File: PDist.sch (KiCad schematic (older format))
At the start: 27 parts

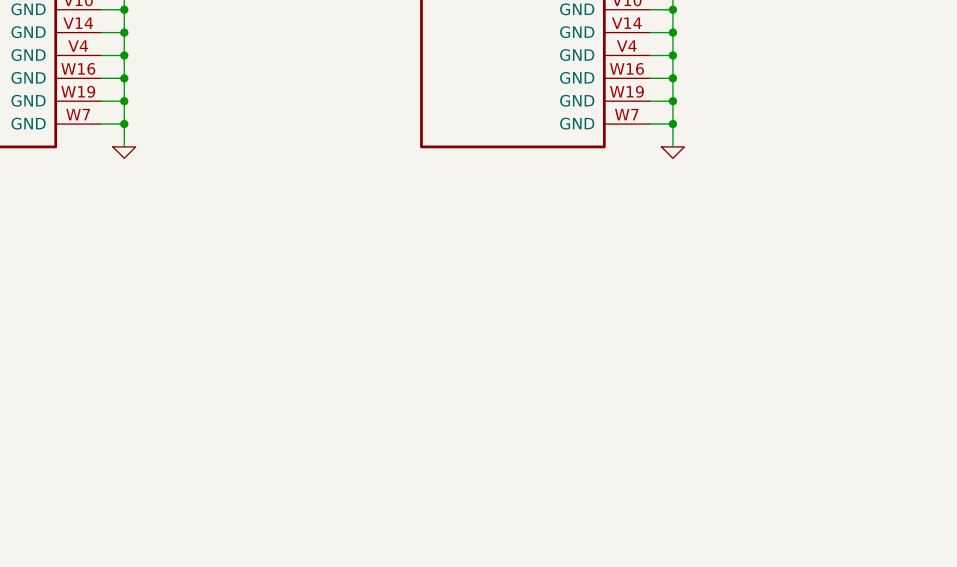
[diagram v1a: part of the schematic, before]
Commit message: Route CPU bus and cache
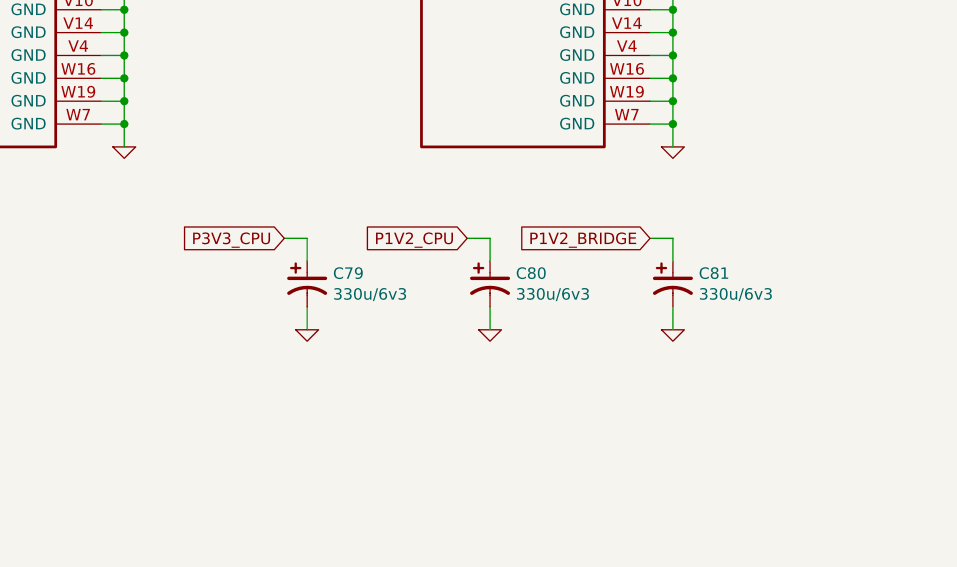
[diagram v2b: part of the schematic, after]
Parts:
- added C79, C80, C81: 330u/6v3, IPC7351-Nominal:CAPMP6032X280, symbol C-TANT-6032-28
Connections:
- net GND: now also C79.2, C80.2, C81.2
- net P1V2_BRIDGE: now also C81.1
- net P1V2_CPU: now also C80.1
- net P3V3_CPU: now also C79.1
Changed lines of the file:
@@
 $EndComp
 $Comp
-L GND #PWR7
+L GND #PWR10
 U 1 1 57647804
 P 1200 6200
-F 0 "#PWR7" H 1200 6200 30  0001 C CNN
+F 0 "#PWR10" H 1200 6200 30  0001 C CNN
 F 1 "GND" H 1200 6130 30  0001 C CNN
 F 2 "" H 1200 6200 60  0000 C CNN
@@
 	6000 6800 5900 6800
 $Comp
-L GND #PWR12
+L GND #PWR15
 U 1 1 57685CC5
 P 6000 6900
-F 0 "#PWR12" H 6000 6900 30  0001 C CNN
+F 0 "#PWR15" H 6000 6900 30  0001 C CNN
 F 1 "GND" H 6000 6830 30  0001 C CNN
 F 2 "" H 6000 6900 60  0000 C CNN
@@
 Connection ~ 2800 7200
 $Comp
-L GND #PWR8
+L GND #PWR11
 U 1 1 5781AB87
 P 1200 7300
-F 0 "#PWR8" H 1200 7300 30  0001 C CNN
+F 0 "#PWR11" H 1200 7300 30  0001 C CNN
 F 1 "GND" H 1200 7230 30  0001 C CNN
 F 2 "" H 1200 7300 60  0000 C CNN
@@
 Connection ~ 2800 7800
 $Comp
-L GND #PWR9
+L GND #PWR12
 U 1 1 5781BEBF
 P 1200 7900
-F 0 "#PWR9" H 1200 7900 30  0001 C CNN
+F 0 "#PWR12" H 1200 7900 30  0001 C CNN
 F 1 "GND" H 1200 7830 30  0001 C CNN
 F 2 "" H 1200 7900 60  0000 C CNN
@@
 Connection ~ 2800 8400
 $Comp
-L GND #PWR10
+L GND #PWR13
 U 1 1 5781BFF0
 P 1200 8500
-F 0 "#PWR10" H 1200 8500 30  0001 C CNN
+F 0 "#PWR13" H 1200 8500 30  0001 C CNN
 F 1 "GND" H 1200 8430 30  0001 C CNN
 F 2 "" H 1200 8500 60  0000 C CNN
@@
 	2800 9300 2800 9200
 $Comp
-L GND #PWR11
+L GND #PWR14
 U 1 1 5781C039
 P 1200 9400
-F 0 "#PWR11" H 1200 9400 30  0001 C CNN
+F 0 "#PWR14" H 1200 9400 30  0001 C CNN
 F 1 "GND" H 1200 9330 30  0001 C CNN
 F 2 "" H 1200 9400 60  0000 C CNN
@@
 	8400 1000 8400 6900
 $Comp
-L GND #PWR13
+L GND #PWR18
 U 1 1 578EB8DE
 P 8400 6900
-F 0 "#PWR13" H 8400 6900 30  0001 C CNN
+F 0 "#PWR18" H 8400 6900 30  0001 C CNN
 F 1 "GND" H 8400 6830 30  0001 C CNN
 F 2 "" H 8400 6900 60  0000 C CNN
@@
 	10800 1000 10800 6900
 $Comp
-L GND #PWR14
+L GND #PWR20
 U 1 1 578EED1F
 P 10800 6900
-F 0 "#PWR14" H 10800 6900 30  0001 C CNN
+F 0 "#PWR20" H 10800 6900 30  0001 C CNN
 F 1 "GND" H 10800 6830 30  0001 C CNN
 F 2 "" H 10800 6900 60  0000 C CNN
@@
 Wire Wire Line
 	9500 1400 9000 1400
+$Comp
+L C-TANT-6032-28 C?
+U 1 1 5793D7F4
+P 6800 7500
+AR Path="/5765B2E6/5793D7F4" Ref="C?"  Part="1"
+AR Path="/5763AB3B/5793D7F4" Ref="C79"  Part="1"
+F 0 "C79" H 6913 7546 50  0000 L CNN
+F 1 "330u/6v3" H 6913 7455 50  0000 L CNN
+F 2 "IPC7351-Nominal:CAPMP6032X280" H 6800 7350 50  0001 C CNN
+F 3 "" H 6790 7475 60  0000 C CNN
+F 4 "DIST DIGIKEY 478-8902-1-ND" H 6800 7250 60  0001 C CNN "BOM"
+	1    6800 7500
+	1    0    0    -1
+$EndComp
+Text GLabel 6700 7300 0    50   Input ~ 0
+P3V3_CPU
+Wire Wire Line
+	6700 7300 6800 7300
+Wire Wire Line
+	6800 7300 6800 7400
+$Comp
+L GND #PWR16
+U 1 1 5793DC64
+P 6800 7700
+F 0 "#PWR16" H 6800 7700 30  0001 C CNN
+F 1 "GND" H 6800 7630 30  0001 C CNN
+F 2 "" H 6800 7700 60  0000 C CNN
+F 3 "" H 6800 7700 60  0000 C CNN
+	1    6800 7700
+	1    0    0    -1
+$EndComp
+Wire Wire Line
+	6800 7700 6800 7600
+Text GLabel 7500 7300 0    50   Input ~ 0
+P1V2_CPU
+$Comp
+L C-TANT-6032-28 C?
+U 1 1 57941170
+P 7600 7500
+AR Path="/5765B2E6/57941170" Ref="C?"  Part="1"
+AR Path="/5763AB3B/57941170" Ref="C80"  Part="1"
+F 0 "C80" H 7713 7546 50  0000 L CNN
+F 1 "330u/6v3" H 7713 7455 50  0000 L CNN
+F 2 "IPC7351-Nominal:CAPMP6032X280" H 7600 7350 50  0001 C CNN
+F 3 "" H 7590 7475 60  0000 C CNN
+F 4 "DIST DIGIKEY 478-8902-1-ND" H 7600 7250 60  0001 C CNN "BOM"
+	1    7600 7500
+	1    0    0    -1
+$EndComp
+Wire Wire Line
+	7500 7300 7600 7300
+Wire Wire Line
+	7600 7300 7600 7400
+$Comp
+L GND #PWR17
+U 1 1 5794152A
+P 7600 7700
+F 0 "#PWR17" H 7600 7700 30  0001 C CNN
+F 1 "GND" H 7600 7630 30  0001 C CNN
+F 2 "" H 7600 7700 60  0000 C CNN
+F 3 "" H 7600 7700 60  0000 C CNN
+	1    7600 7700
+	1    0    0    -1
+$EndComp
+Wire Wire Line
+	7600 7700 7600 7600
+Text GLabel 8300 7300 0    50   Input ~ 0
+P1V2_BRIDGE
+$Comp
+L C-TANT-6032-28 C?
+U 1 1 57941998
+P 8400 7500
+AR Path="/5765B2E6/57941998" Ref="C?"  Part="1"
+AR Path="/5763AB3B/57941998" Ref="C81"  Part="1"
+F 0 "C81" H 8513 7546 50  0000 L CNN
+F 1 "330u/6v3" H 8513 7455 50  0000 L CNN
+F 2 "IPC7351-Nominal:CAPMP6032X280" H 8400 7350 50  0001 C CNN
+F 3 "" H 8390 7475 60  0000 C CNN
+F 4 "DIST DIGIKEY 478-8902-1-ND" H 8400 7250 60  0001 C CNN "BOM"
+	1    8400 7500
+	1    0    0    -1
+$EndComp
+Wire Wire Line
+	8300 7300 8400 7300
+Wire Wire Line
+	8400 7300 8400 7400
+$Comp
+L GND #PWR19
+U 1 1 57941D48
+P 8400 7700
+F 0 "#PWR19" H 8400 7700 30  0001 C CNN
+F 1 "GND" H 8400 7630 30  0001 C CNN
+F 2 "" H 8400 7700 60  0000 C CNN
+F 3 "" H 8400 7700 60  0000 C CNN
+	1    8400 7700
+	1    0    0    -1
+$EndComp
+Wire Wire Line
+	8400 7700 8400 7600
 $EndSCHEMATC

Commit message: workworkwork
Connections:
- net P1V2_CPU is gone; now on net P1V2_CORE: C80.1, CPU0.K13 (VCCINT), CPU0.K9 (VCCINT), CPU0.L10 (VCCINT), CPU0.L12 (VCCINT), CPU0.L14 (VCCINT), CPU0.M11 (VCCINT), CPU0.M13 (VCCINT), CPU0.M9 (VCCINT), CPU0.N10 (VCCINT), CPU0.N12 (VCCINT), CPU0.N14 (VCCINT), CPU0.P11 (VCCINT), CPU0.P13 (VCCINT), CPU0.P9 (VCCINT), CPU0.R14 (VCCINT), CPU1.K13 (VCCINT), CPU1.K9 (VCCINT), CPU1.L10 (VCCINT), CPU1.L12 (VCCINT), CPU1.L14 (VCCINT), CPU1.M11 (VCCINT), CPU1.M13 (VCCINT), CPU1.M9 (VCCINT), CPU1.N10 (VCCINT), CPU1.N12 (VCCINT), CPU1.N14 (VCCINT), CPU1.P11 (VCCINT), CPU1.P13 (VCCINT), CPU1.P9 (VCCINT), CPU1.R14 (VCCINT)
- net P1V2_BRIDGE renamed P1V2_CORE
- net P1V2_CORE: no longer C81.1
- new net P1V5_BRIDGE: C81.1
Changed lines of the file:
@@
 $Descr B 17000 11000
 encoding utf-8
-Sheet 2 9
+Sheet 2 10
 Title ""
 Date ""
@@
 	4600 1500 4600 2800
 Text GLabel 4500 2900 0    50   Input ~ 0
-P1V2_BRIDGE
+P1V2_CORE
 Wire Wire Line
 	4600 2900 4600 4800
@@
 P3V3_CPU
 Text GLabel 6900 2900 0    50   Input ~ 0
-P1V2_CPU
+P1V2_CORE
 Wire Wire Line
 	6900 2900 7100 2900
@@
 P3V3_CPU
 Text GLabel 9300 2900 0    50   Input ~ 0
-P1V2_CPU
+P1V2_CORE
 Wire Wire Line
 	9300 2900 9500 2900
@@
 	6800 7700 6800 7600
 Text GLabel 7500 7300 0    50   Input ~ 0
-P1V2_CPU
+P1V2_CORE
 $Comp
 L C-TANT-6032-28 C?
@@
 	7600 7700 7600 7600
 Text GLabel 8300 7300 0    50   Input ~ 0
-P1V2_BRIDGE
+P1V5_BRIDGE
 $Comp
 L C-TANT-6032-28 C?

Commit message: power, yo
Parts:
- added C90, C91, C92, C93, C94, C95, C96, C97: 1u, IPC7351-Nominal:CAPC1005X55, symbol C-0402
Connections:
- net P1V5_RAM is gone; now on net P1V5_BRIDGE: C10.1, C11.1, C12.1, C14.1, C15.1, C16.1, C18.1, C19.1, C20.1, C22.1, C23.1, C24.1, C26.1, C27.1, C28.1, C30.1, C31.1, C32.1, SODIMM1.100 (VDD), SODIMM1.105 (VDD), SODIMM1.106 (VDD), SODIMM1.111 (VDD), SODIMM1.112 (VDD), SODIMM1.117 (VDD), SODIMM1.118 (VDD), SODIMM1.123 (VDD), SODIMM1.124 (VDD), SODIMM1.75 (VDD), SODIMM1.76 (VDD), SODIMM1.81 (VDD), SODIMM1.82 (VDD), SODIMM1.87 (VDD), SODIMM1.88 (VDD), SODIMM1.93 (VDD), SODIMM1.94 (VDD), SODIMM1.99 (VDD)
- net GND: now also C90.2, C91.2, C92.2, C93.2, C94.2, C95.2, C96.2, C97.2
- net P1V2_CORE: now also C90.1, C91.1, C92.1, C93.1, C94.1, C95.1, C96.1, C97.1
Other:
- note added: "BRIDGE CORE"

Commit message: TODO: learn to write good commit messages
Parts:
- added J3, J4, J5: JTAG, conn-fci:98424-G52-14ALF, symbol CONN-100MIL-M-2x7-SHROUD
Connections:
- net BR_TCK: now also J3.6
- net BR_TDI: now also J3.10
- net BR_TDO: now also J3.8
- net BR_TMS: now also J3.4
- net CPU0_TCK: now also J4.6
- net CPU0_TDI: now also J4.10
- net CPU0_TDO: now also J4.8
- net CPU0_TMS: now also J4.4
- net CPU1_TCK: now also J5.6
- net CPU1_TDI: now also J5.10
- net CPU1_TDO: now also J5.8
- net CPU1_TMS: now also J5.4
- net GND: now also J3.1, J3.11, J3.13, J3.3, J3.5, J3.7, J3.9, J4.1, J4.11, J4.13, J4.3, J4.5, J4.7, J4.9, J5.1, J5.11, J5.13, J5.3, J5.5, J5.7, J5.9
- net P3V3_BRIDGE: now also J3.2
- net P3V3_CPU: now also J4.2, J5.2
- net PV75_VREF renamed PV75_SDRAM_VREF
- net PV75_VTT renamed PV75_SDRAM_VTT
- no-connect marks 0 -> 6

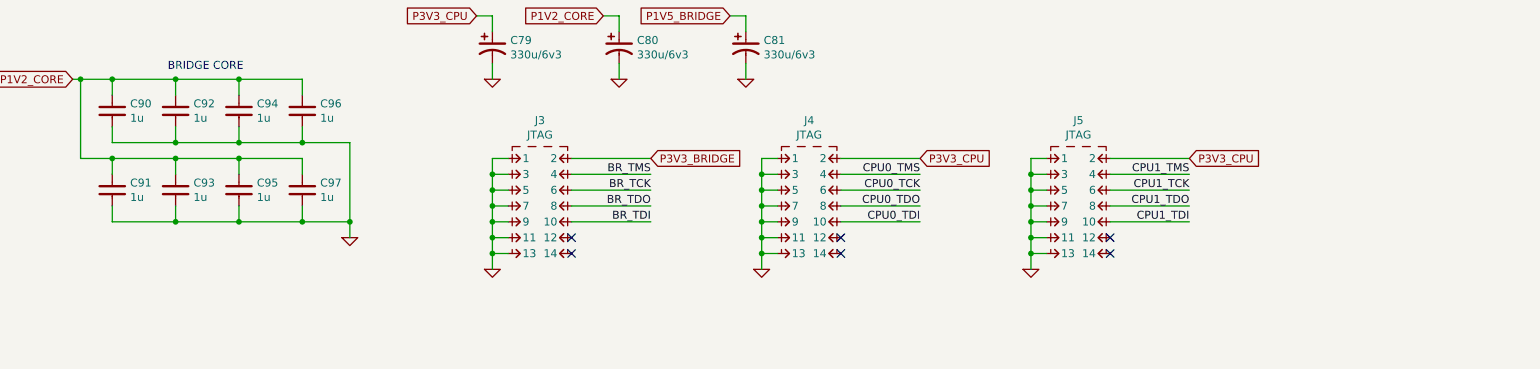
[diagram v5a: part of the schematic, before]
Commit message: Add configuration pullup resistors
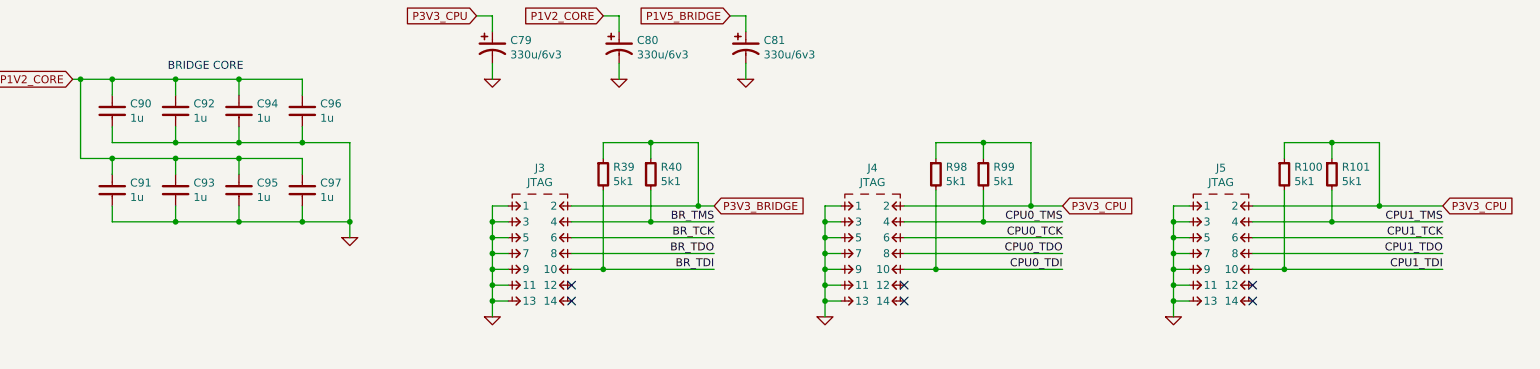
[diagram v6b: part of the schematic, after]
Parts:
- added R100, R101, R39, R40, R98, R99: 5k1, IPC7351-Nominal:RESC1005X40, symbol R-0402
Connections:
- net BR_TDI: now also R39.2
- net BR_TMS: now also R40.2
- net CPU0_TDI: now also R98.2
- net CPU0_TMS: now also R99.2
- net CPU1_TDI: now also R100.2
- net CPU1_TMS: now also R101.2
- net P3V3_BRIDGE: now also R39.1, R40.1
- net P3V3_CPU: now also R100.1, R101.1, R98.1, R99.1
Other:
- moved on the sheet: J3, J4, J5

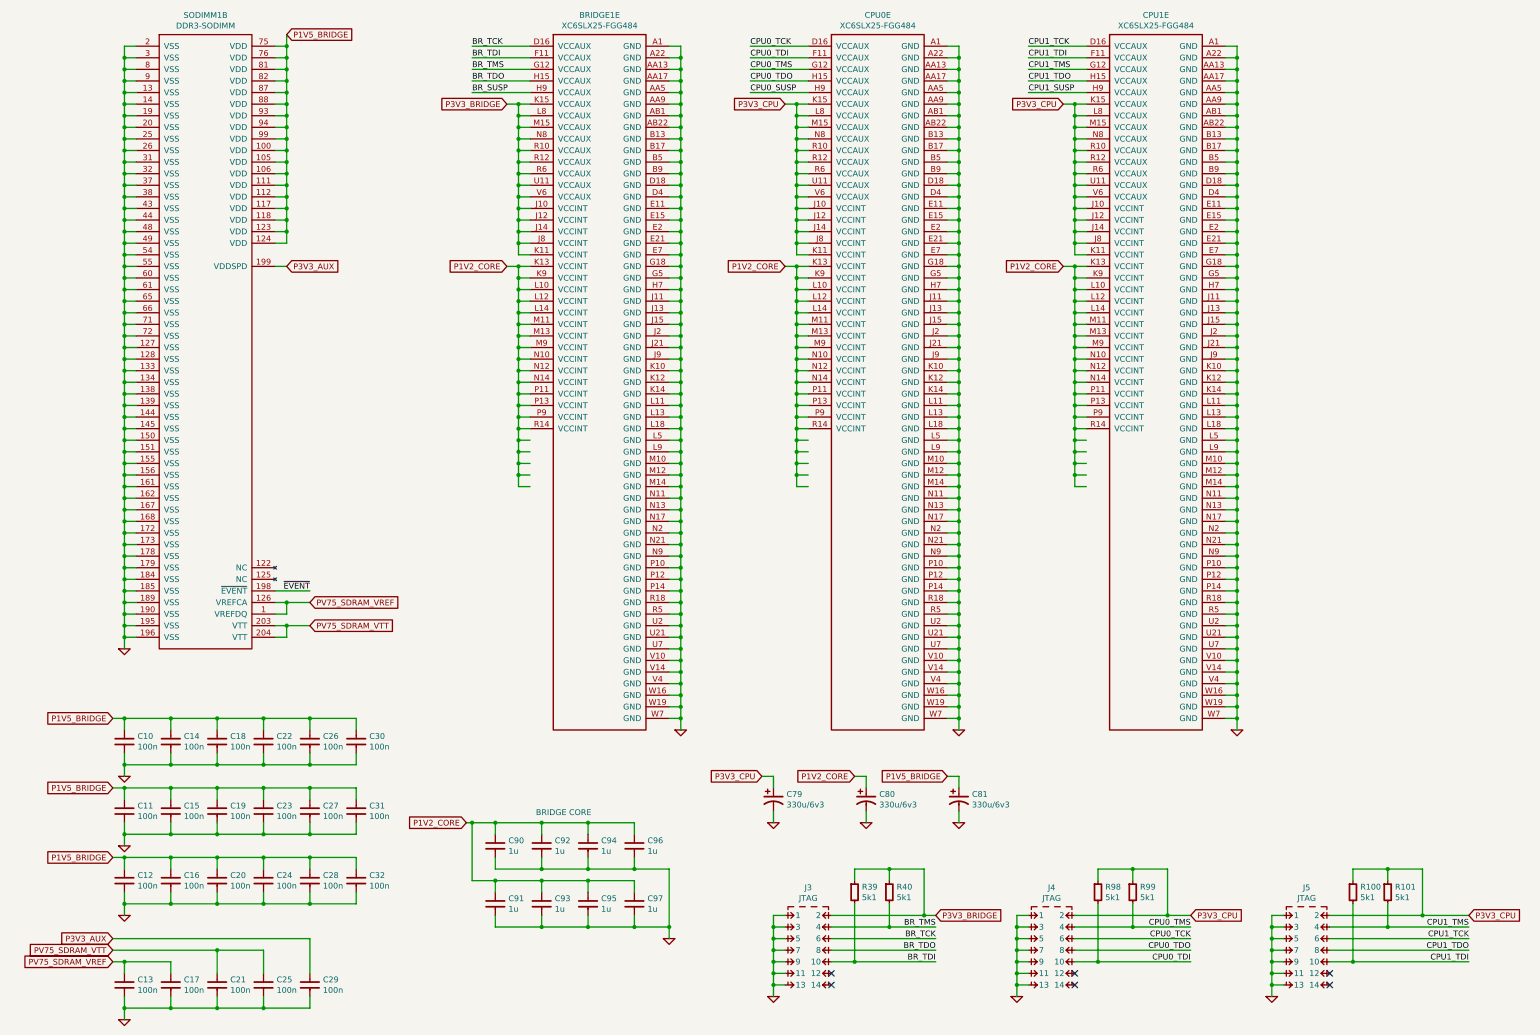
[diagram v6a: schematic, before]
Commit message: Tidy up Power Distribution page
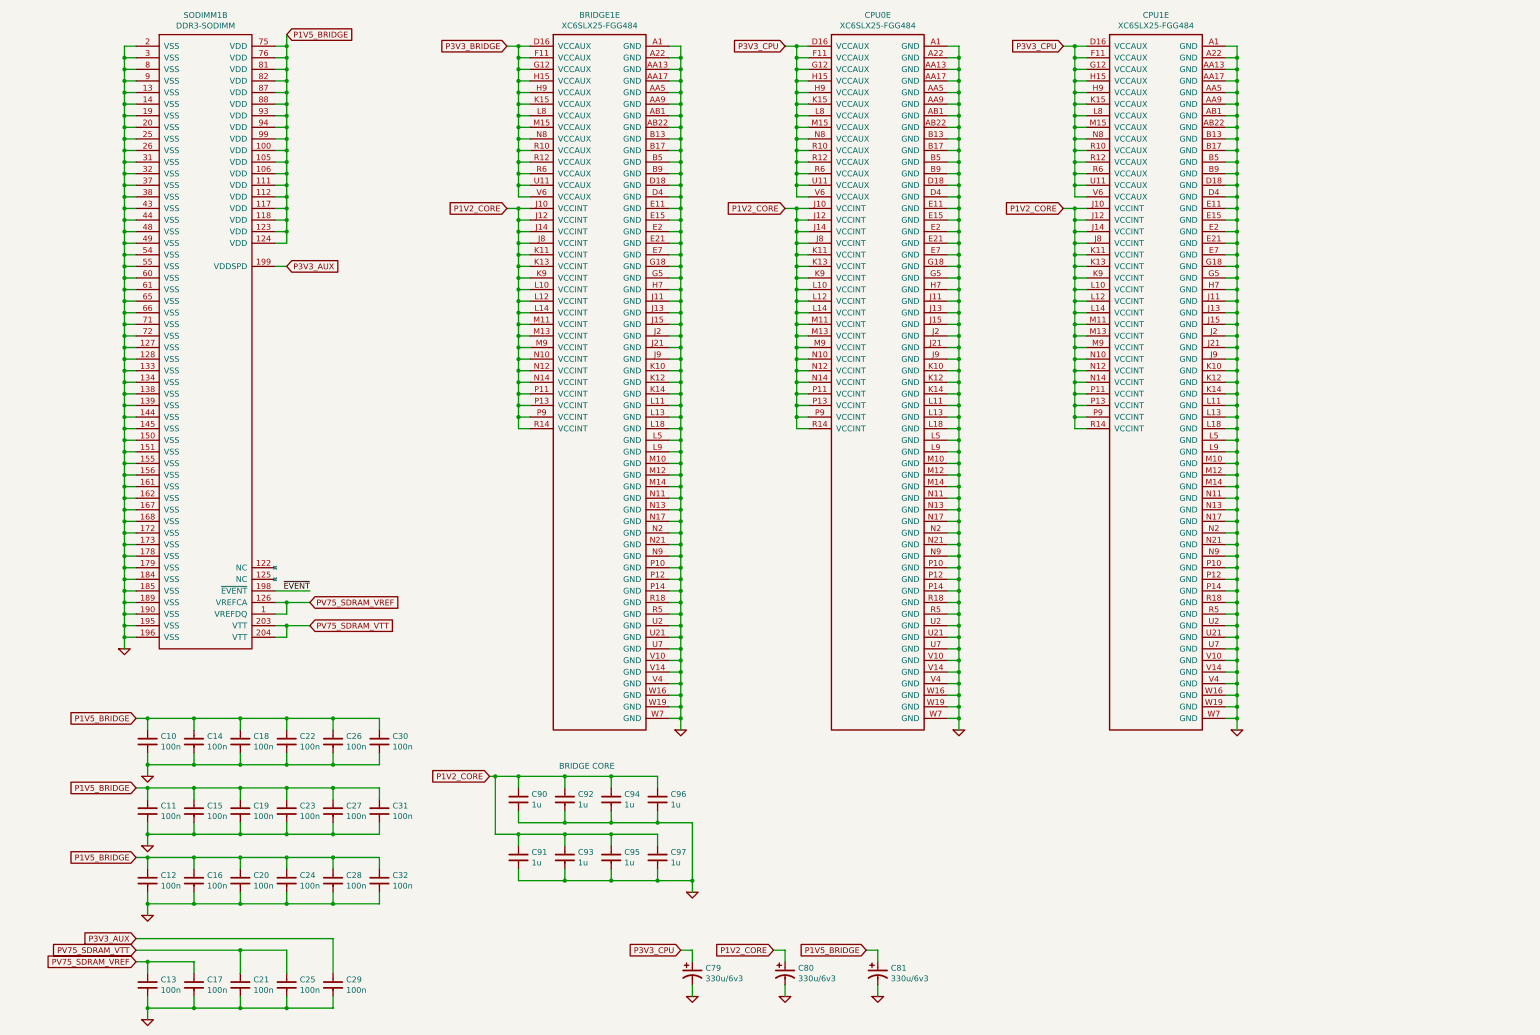
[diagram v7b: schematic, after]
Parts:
- removed J3, J4, J5: JTAG, conn-fci:98424-G52-14ALF, symbol CONN-100MIL-M-2x7-SHROUD
- removed R100, R101, R39, R40, R98, R99: 5k1, IPC7351-Nominal:RESC1005X40, symbol R-0402
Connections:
- net BR_SUSP is gone; now on net P3V3_BRIDGE: BRIDGE1.H9 (VCCAUX)
- net BR_TCK is gone; now on net P3V3_BRIDGE: BRIDGE1.D16 (VCCAUX)
- net BR_TDI is gone; now on net P3V3_BRIDGE: BRIDGE1.F11 (VCCAUX)
- net BR_TDO is gone; now on net P3V3_BRIDGE: BRIDGE1.H15 (VCCAUX)
- net BR_TMS is gone; now on net P3V3_BRIDGE: BRIDGE1.G12 (VCCAUX)
- net CPU0_SUSP is gone; now on net P3V3_CPU: CPU0.H9 (VCCAUX)
- net CPU0_TCK is gone; now on net P3V3_CPU: CPU0.D16 (VCCAUX)
- net CPU0_TDI is gone; now on net P3V3_CPU: CPU0.F11 (VCCAUX)
- net CPU0_TDO is gone; now on net P3V3_CPU: CPU0.H15 (VCCAUX)
- net CPU0_TMS is gone; now on net P3V3_CPU: CPU0.G12 (VCCAUX)
- net CPU1_SUSP is gone; now on net P3V3_CPU: CPU1.H9 (VCCAUX)
- net CPU1_TCK is gone; now on net P3V3_CPU: CPU1.D16 (VCCAUX)
- net CPU1_TDI is gone; now on net P3V3_CPU: CPU1.F11 (VCCAUX)
- net CPU1_TDO is gone; now on net P3V3_CPU: CPU1.H15 (VCCAUX)
- net CPU1_TMS is gone; now on net P3V3_CPU: CPU1.G12 (VCCAUX)
- net P1V2_CORE: now also BRIDGE1.J10 (VCCINT), BRIDGE1.J12 (VCCINT), BRIDGE1.J14 (VCCINT), BRIDGE1.J8 (VCCINT), BRIDGE1.K11 (VCCINT), CPU0.J10 (VCCINT), CPU0.J12 (VCCINT), CPU0.J14 (VCCINT), CPU0.J8 (VCCINT), CPU0.K11 (VCCINT), CPU1.J10 (VCCINT), CPU1.J12 (VCCINT), CPU1.J14 (VCCINT), CPU1.J8 (VCCINT), CPU1.K11 (VCCINT)
- net P3V3_BRIDGE: no longer BRIDGE1.J10 (VCCINT), BRIDGE1.J12 (VCCINT), BRIDGE1.J14 (VCCINT), BRIDGE1.J8 (VCCINT), BRIDGE1.K11 (VCCINT)
- net P3V3_CPU: no longer CPU0.J10 (VCCINT), CPU0.J12 (VCCINT), CPU0.J14 (VCCINT), CPU0.J8 (VCCINT), CPU0.K11 (VCCINT), CPU1.J10 (VCCINT), CPU1.J12 (VCCINT), CPU1.J14 (VCCINT), CPU1.J8 (VCCINT), CPU1.K11 (VCCINT)
- no-connect marks 6 -> 0
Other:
- moved on the sheet: C10, C11, C12, C13, C14, C15, C16, C17, C18, C19, C20, C21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
